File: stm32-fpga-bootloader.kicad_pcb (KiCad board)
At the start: 2 copper layers, 100 x 100 mm, 166 parts, among them J1 USB_C_Receptacle_USB2.0_14P, J10 LEDX, J11 LEDY, J12 PMOD, J13 Raspberry_Pi_2_3, J14 CPLD_JTAG, J2 Conn_01x02, J3 RPI-TO-CPLD, J5 PMOD, J6 Conn_01x02, J7 TO-LCD, J8 USB_C_Receptacle_USB2.0_14P, Q1 2N7002K, Q2 2N7002K, Q3 2N7002K, SW1 BOOT, SW2 RUN, SW3 ICE_BTN, SW4 ICE_RST, SW5 BOOT, U1 AMS1117-3.3, U10 RP2040, U2 W25Q128JVS, U3 LMV321, U4 ACPL-798J-500E, U5 ICE40UP5K-SG48ITR, U6 W25Q128JVS, U7 LP5907MFX-1.2, U8 MAX7221xNG, U9 LCMXO2-1200HC-4TG100I, Y1 12Mhz

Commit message: Update the source files
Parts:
- added C47: 4.7u, Capacitor_SMD:C_0603_1608Metric, F.Cu at (139.0, 120.0)
- added J4001: Conn_01x08, Connector_PinSocket_2.54mm:PinSocket_1x08_P2.54mm_Vertical, F.Cu at (159.3, 103.2)
- added Q4: 2N7002K, Package_TO_SOT_SMD:SOT-23, F.Cu at (122.2, 111.9)
- added Q5: 2N7002K, Package_TO_SOT_SMD:SOT-23, F.Cu at (143.5, 112.2)
- added Q6: 2N7002K, Package_TO_SOT_SMD:SOT-23, F.Cu at (126.6, 112.0)
- added Q7: 2N7002K, Package_TO_SOT_SMD:SOT-23, F.Cu at (147.6, 112.2)
- added R63: 10k, Resistor_SMD:R_0402_1005Metric, F.Cu at (135.9, 119.9)
- added R64: 10k, Resistor_SMD:R_0402_1005Metric, F.Cu at (123.0, 109.4)
- added R65: 330R, Resistor_SMD:R_0402_1005Metric, F.Cu at (123.0, 114.4)
- added R66: 330R, Resistor_SMD:R_0402_1005Metric, F.Cu at (144.3, 114.6)
- added R67: 10k, Resistor_SMD:R_0402_1005Metric, F.Cu at (144.3, 109.8)
- added R68: 10k, Resistor_SMD:R_0402_1005Metric, F.Cu at (125.8, 114.4)
- added R69: 330R, Resistor_SMD:R_0402_1005Metric, F.Cu at (125.8, 109.6)
- added R70: 10k, Resistor_SMD:R_0402_1005Metric, F.Cu at (148.3, 109.8)
- added R71: 330R, Resistor_SMD:R_0402_1005Metric, F.Cu at (148.3, 114.7)
- added TP1: TestPoint, TestPoint:TestPoint_Pad_1.0x1.0mm, F.Cu at (131.1, 120.3)
- added U11: 74HC595D, PCM_JLCPCB:SOIC-16_3.9x9.9mm_P1.27mm, F.Cu at (135.5, 112.1)
- added U12: LTC-3743KD, KiCadLocal:LTC-3743KD, F.Cu at (126.6, 117.2)
- moved C16 64.2 mm to (210.2, 87.1), turned to -90 degrees
- moved C15 43.2 mm to (208.8, 87.0), turned to -90 degrees
- moved C2 37.2 mm to (124.1, 83.4), turned to 180 degrees
- moved U2 30.3 mm to (125.7, 88.7), turned to 90 degrees
- moved R3 27.0 mm to (123.8, 94.5), turned to 0 degrees
- moved D11 26.9 mm to (116.6, 75.7)
- moved R6 26.6 mm to (120.1, 76.0)
- moved C10 23.4 mm to (141.8, 91.2)
- moved C44 23.4 mm to (137.8, 83.2)
- moved C7 23.4 mm to (144.0, 94.6)
- moved R1 23.4 mm to (130.7, 86.6)
- moved R12 23.4 mm to (141.8, 83.5)
- moved R2 23.4 mm to (130.8, 87.8)
- moved Y1 23.4 mm to (144.5, 88.1)
- moved C3 23.4 mm to (152.0, 83.3)
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
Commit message: Update the schematic
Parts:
- removed J4001: Conn_01x08, Connector_PinSocket_2.54mm:PinSocket_1x08_P2.54mm_Vertical
- added C48: 100n, Capacitor_SMD:C_0402_1005Metric, F.Cu at (122.6, 76.1)
- added C49: 10uF, Capacitor_SMD:C_0603_1608Metric, F.Cu at (125.5, 67.1)
- added J15: Conn_01x02, TerminalBlock_Phoenix:TerminalBlock_Phoenix_PT-1,5-2-3.5-H_1x02_P3.50mm_Horizontal, F.Cu at (117.9, 68.8)
- added J9: PMOD, Connector_PinSocket_2.54mm:PinSocket_2x06_P2.54mm_Vertical, F.Cu at (166.0, 78.0)
- added R72: 10k, Resistor_SMD:R_0402_1005Metric, F.Cu at (126.0, 131.8)
- added R73: 1.2K, Resistor_SMD:R_0603_1608Metric, F.Cu at (125.5, 69.6)
- added R74: 1.2K, Resistor_SMD:R_0603_1608Metric, F.Cu at (125.5, 72.1)
- added R75: 1.2K, Resistor_SMD:R_0603_1608Metric, F.Cu at (125.5, 74.6)
- added R76: 1.2K, Resistor_SMD:R_0603_1608Metric, F.Cu at (129.5, 67.1)
- added R77: 1.2K, Resistor_SMD:R_0603_1608Metric, F.Cu at (129.5, 69.6)
- added R78: 100R, Resistor_SMD:R_0603_1608Metric, F.Cu at (129.5, 72.1)
- added R79: 100R, Resistor_SMD:R_0603_1608Metric, F.Cu at (129.5, 74.6)
- added R80: 100R, Resistor_SMD:R_0603_1608Metric, F.Cu at (133.5, 67.1)
- added R81: 100R, Resistor_SMD:R_0603_1608Metric, F.Cu at (133.5, 69.6)
- added R82: 100R, Resistor_SMD:R_0603_1608Metric, F.Cu at (133.5, 72.1)
- added R83: 100R, Resistor_SMD:R_0603_1608Metric, F.Cu at (133.5, 74.6)
- added U1001: XC6206PxxxMR, Package_TO_SOT_SMD:SOT-23-3, F.Cu at (142.8, 120.6)
- added U13: ACPL-798J-500E, EasyEDA_Lib:SO-16_L10.3-W7.5-P1.27-LS10.6-BL, B.Cu at (129.9, 70.7)
- moved J2 90.6 mm to (226.0, 94.0)
- moved R13 74.6 mm to (244.8, 95.3)
- moved R15 74.6 mm to (248.2, 77.6)
- moved C11 74.6 mm to (236.7, 85.6)
- moved C12 74.6 mm to (236.7, 87.6)
- moved R14 74.6 mm to (234.3, 99.0)
- moved R16 74.6 mm to (248.2, 80.2)
- moved R17 74.6 mm to (234.3, 101.0)
- moved U3 74.6 mm to (232.7, 87.0)
- moved R18 74.6 mm to (234.3, 103.0)
- moved Q4 28.1 mm to (121.5, 83.8)
- moved Q5 28.1 mm to (142.8, 84.1)
- moved R63 28.1 mm to (135.2, 91.8)
- moved R64 28.1 mm to (122.3, 81.3)
- moved R65 28.1 mm to (122.3, 86.3)
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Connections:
- A2 pad 14: /CPLDK_SCK -> /CPLD_CLOCK
- U1 pad 1: GND -> unconnected-(U1-GND-Pad1)
- U1 pad 2: +3.3V_JTAG -> unconnected-(U1-VO-Pad2)
- U1 pad 3: /jtag-prog/VBUS -> unconnected-(U1-VI-Pad3)

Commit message: Update the schematic
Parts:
- removed J2: Conn_01x02, TerminalBlock_Phoenix:TerminalBlock_Phoenix_PT-1,5-2-3.5-H_1x02_P3.50mm_Horizontal
- added C50: 10uF, Capacitor_SMD:C_0603_1608Metric, F.Cu at (145.7, 66.8)
- added C51: 10uF, Capacitor_SMD:C_0603_1608Metric, F.Cu at (141.5, 66.7)
- added D1003: B5817W, PCM_JLCPCB:D_SOD-123, F.Cu at (137.5, 67.2)
- added D1004: B5817W, PCM_JLCPCB:D_SOD-123, F.Cu at (137.5, 69.7)
- added D1005: B5817W, PCM_JLCPCB:D_SOD-123, F.Cu at (137.5, 72.3)
- added J1001: DATA, Connector_PinSocket_2.54mm:PinSocket_1x04_P2.54mm_Vertical, F.Cu at (132.5, 67.1)
- J15: footprint TerminalBlock_Phoenix:TerminalBlock_Phoenix_PT-1,5-2-3.5-H_1x02_P3.50mm_Horizontal -> Connector_PinSocket_2.54mm:PinSocket_1x02_P2.54mm_Vertical
- U11: footprint PCM_JLCPCB:SOIC-16_3.9x9.9mm_P1.27mm -> PCM_JLCPCB:SOIC-16_L9.9-W3.9-P1.27-LS6.0-BL
- moved R16 94.9 mm to (153.3, 79.8)
- moved R13 94.2 mm to (151.5, 82.5)
- moved R15 92.0 mm to (156.5, 85.1)
- moved R14 82.6 mm to (153.0, 84.5)
- moved R17 82.6 mm to (153.0, 86.5)
- moved R18 82.6 mm to (153.0, 88.5)
- moved C11 78.2 mm to (158.6, 80.8)
- moved C12 78.2 mm to (158.6, 82.8)
- moved U3 78.2 mm to (154.6, 82.2)
- moved U1 35.0 mm to (143.6, 72.1)
- moved U1001 16.2 mm to (150.8, 106.5)
- moved R73 10.5 mm to (115.6, 66.0)
- moved R77 10.1 mm to (119.7, 72.0), turned to -90 degrees
- moved C49 9.58 mm to (128.1, 76.3), turned to 180 degrees
- moved R74 8.94 mm to (119.0, 65.9)
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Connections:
- net /jtag-prog/VBUS renamed VBUS3
- A1 pad 40: unconnected-(A1-VBUS-Pad40) -> VBUS1
- A2 pad 40: unconnected-(A2-VBUS-Pad40) -> VBUS2
- U1 pad 1: unconnected-(U1-GND-Pad1) -> GND
- U1 pad 2: unconnected-(U1-VO-Pad2) -> Net-(U1-VO)
- U1 pad 3: unconnected-(U1-VI-Pad3) -> Net-(U1-VI)

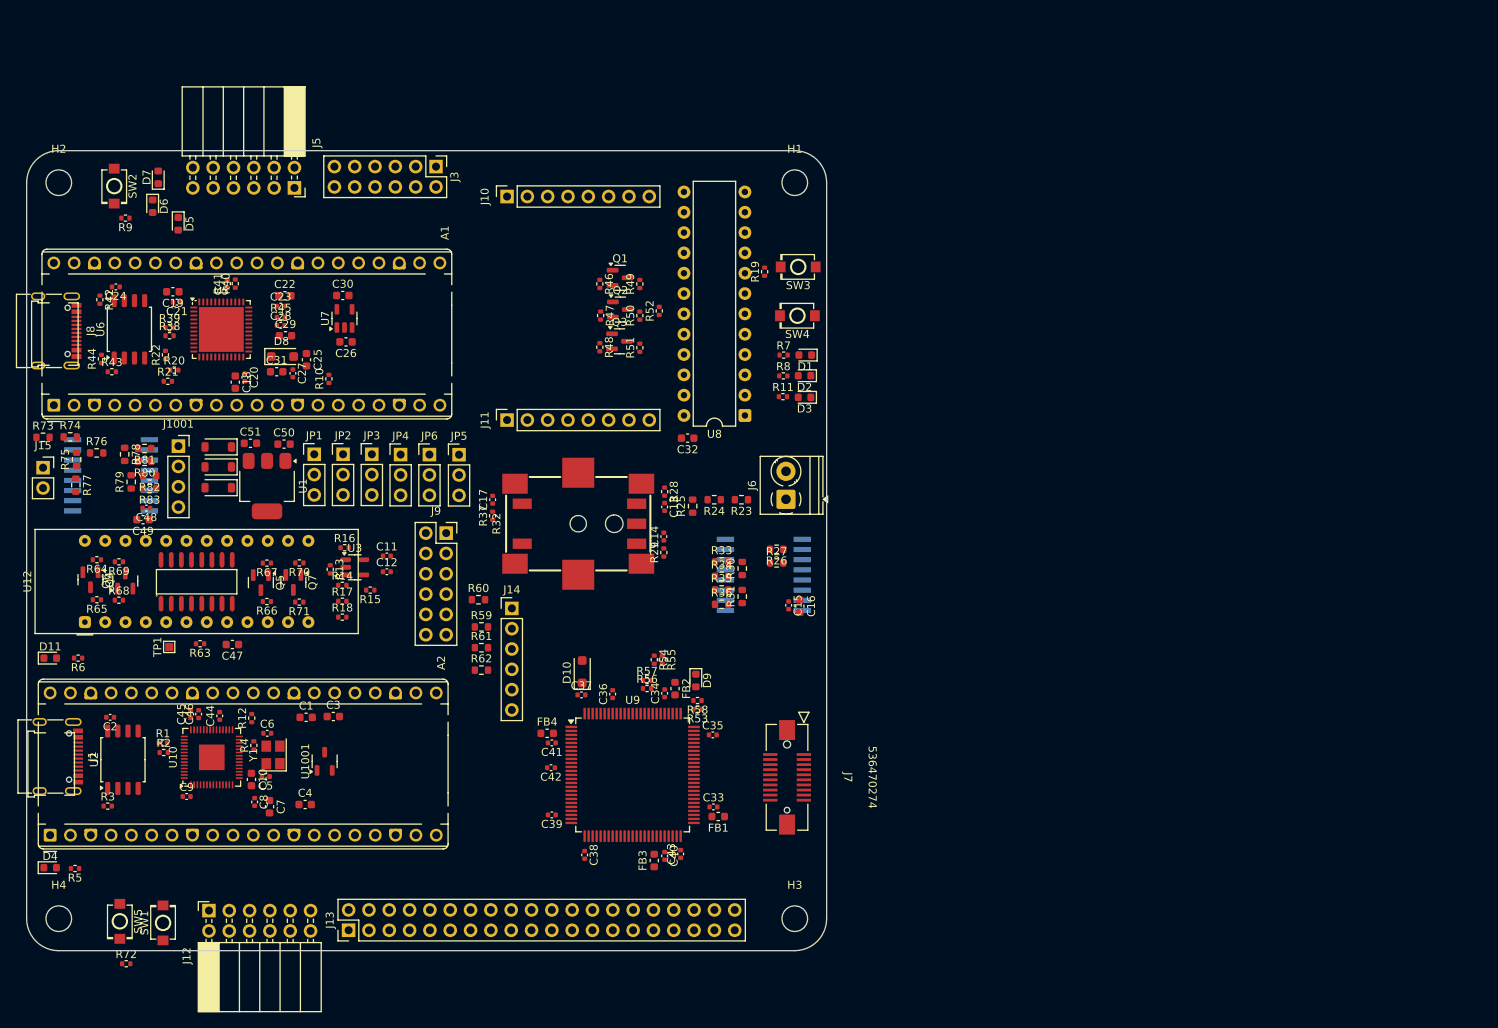
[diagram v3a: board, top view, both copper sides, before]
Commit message: Update the footprints
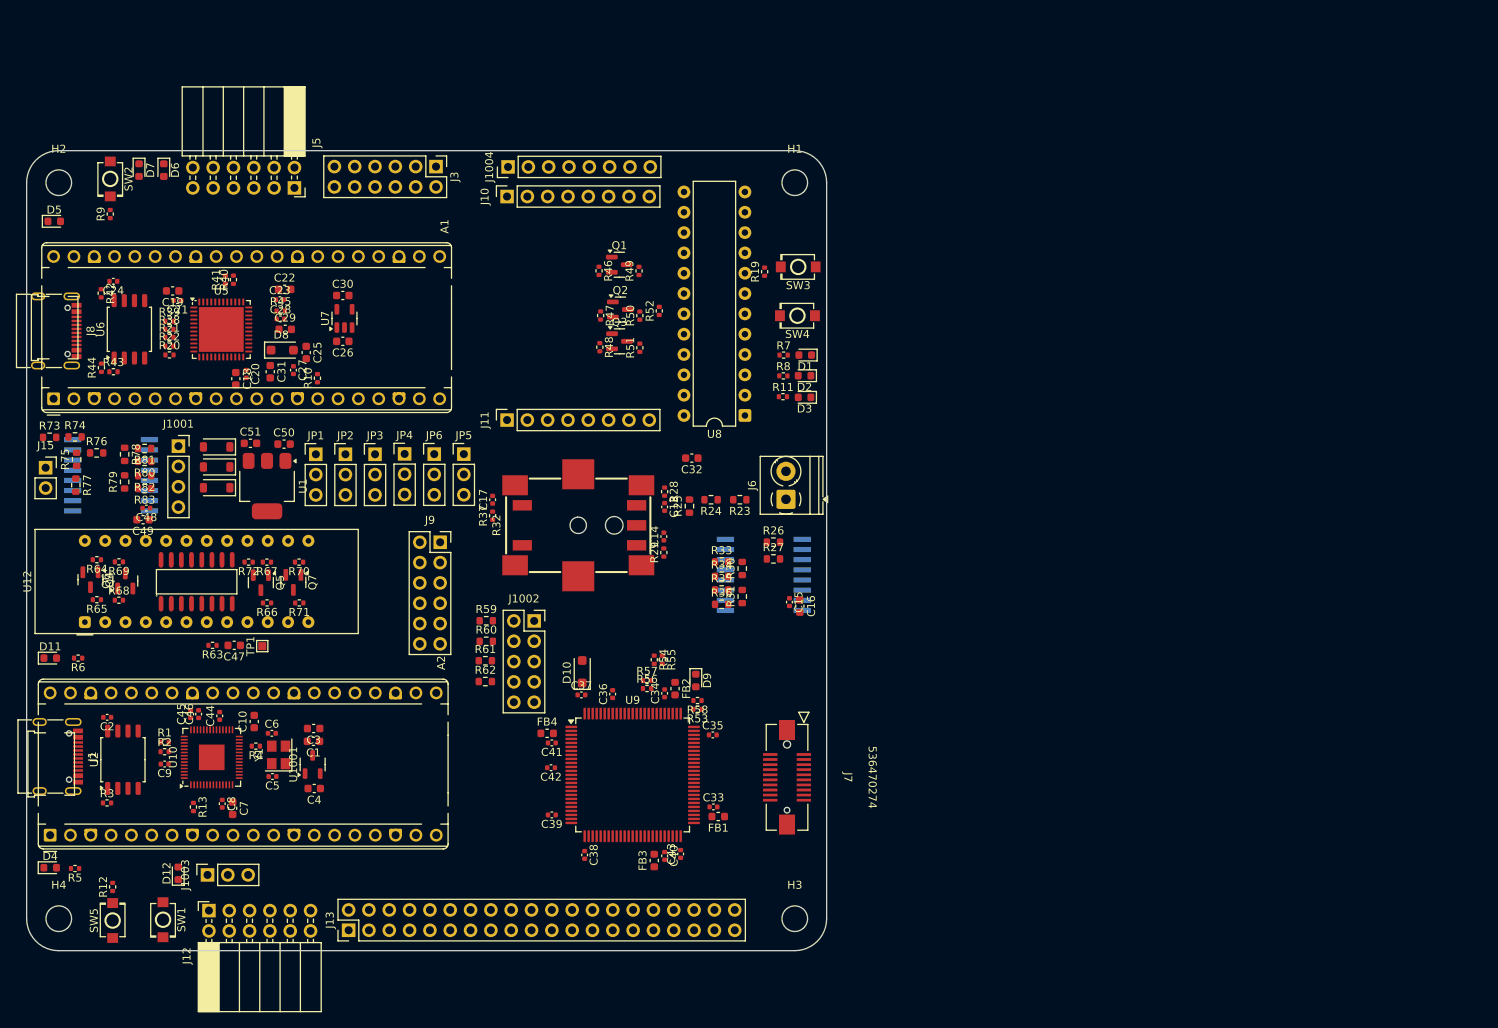
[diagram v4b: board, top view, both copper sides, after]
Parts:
- removed C11, C12: 100n, Capacitor_SMD:C_0402_1005Metric
- removed J14: CPLD_JTAG, Connector_PinHeader_2.54mm:PinHeader_1x06_P2.54mm_Vertical
- removed R14, R15, R16, R17, R18: 1.2K, Resistor_SMD:R_0402_1005Metric
- removed U3: LMV321, Package_TO_SOT_SMD:SOT-23-5
- added D12: RED, LED_SMD:LED_0603_1608Metric, F.Cu at (132.5, 120.5)
- added J1002: JTAG JUMP, Connector_PinSocket_2.54mm:PinSocket_2x05_P2.54mm_Vertical, F.Cu at (177.0, 88.9)
- added J1003: JTAG-LOG, Connector_PinSocket_2.54mm:PinSocket_1x03_P2.54mm_Vertical, F.Cu at (136.2, 120.7)
- added J1004: Conn_01x08, Connector_PinHeader_2.54mm:PinHeader_1x08_P2.54mm_Vertical, F.Cu at (173.7, 32.2)
- R13: value 1R -> 1.2K
- moved R72 52.5 mm to (141.3, 81.6), turned to 180 degrees
- moved R13 34.3 mm to (134.4, 112.2)
- moved R12 27.3 mm to (124.3, 122.2)
- moved D5 15.5 mm to (117.0, 39.0), turned to 0 degrees
- moved TP1 11.6 mm to (143.0, 92.1)
- moved C10 7.26 mm to (142.0, 101.5), turned to 90 degrees
- moved R21 5.50 mm to (131.4, 53.5)
- moved R60 5.29 mm to (171.0, 91.5)
- moved C9 4.90 mm to (130.8, 106.8), turned to 180 degrees
- moved D6 4.72 mm to (130.7, 32.6)
- moved C7 4.62 mm to (139.3, 112.4)
- moved C8 4.06 mm to (138.0, 111.8)
- moved C1 3.14 mm to (149.4, 104.0), turned to 180 degrees
- moved C3 2.88 mm to (149.4, 102.4), turned to 180 degrees
- moved D7 2.56 mm to (127.6, 32.6), turned to -90 degrees
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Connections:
- A1 pad 11: /UART1_TX -> /IOB_23b
- A1 pad 12: /UART1_RX -> /IOT_43a
- A1 pad 33: GND -> unconnected-(A1-AGND-Pad33)
- A1 pad 34: unconnected-(A1-GPIO28_ADC2-Pad34) -> /LED1
- C50 pad 1: Net-(U1-VO) -> +3.3V
- C51 pad 1: Net-(U1-VI) -> +5V
- D1003 pad 1: Net-(U1-VI) -> +5V
- D1004 pad 1: Net-(U1-VI) -> +5V
- D1005 pad 1: Net-(U1-VI) -> +5V
- R11 pad 1: /LED2 -> /IOT_50b
- R13 pad 1: Net-(R13-Pad1) -> /jtag-prog/LED2
- R32 pad A: /ENCODER_B -> /ENCODER_A
- R32 pad B: /ENCODER_A -> /ENCODER_B
- R32 pad D: GND -> /ENCODER_BTN
- R32 pad E: /ENCODER_BTN -> GND
- R59 pad 2: /PT10D/TDI -> /TDI
- R60 pad 2: /PT10C/TDO -> /TDO
- R61 pad 2: /PT11C/TCK -> /TCK
- R62 pad 2: /PT11D/TMS -> /TMS
- U1 pad 2: Net-(U1-VO) -> +3.3V
- U1 pad 3: Net-(U1-VI) -> +5V
- U10 pad 2: unconnected-(U10-GPIO0-Pad2) -> /jtag-prog/LED2

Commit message: Update the BOM and the routing
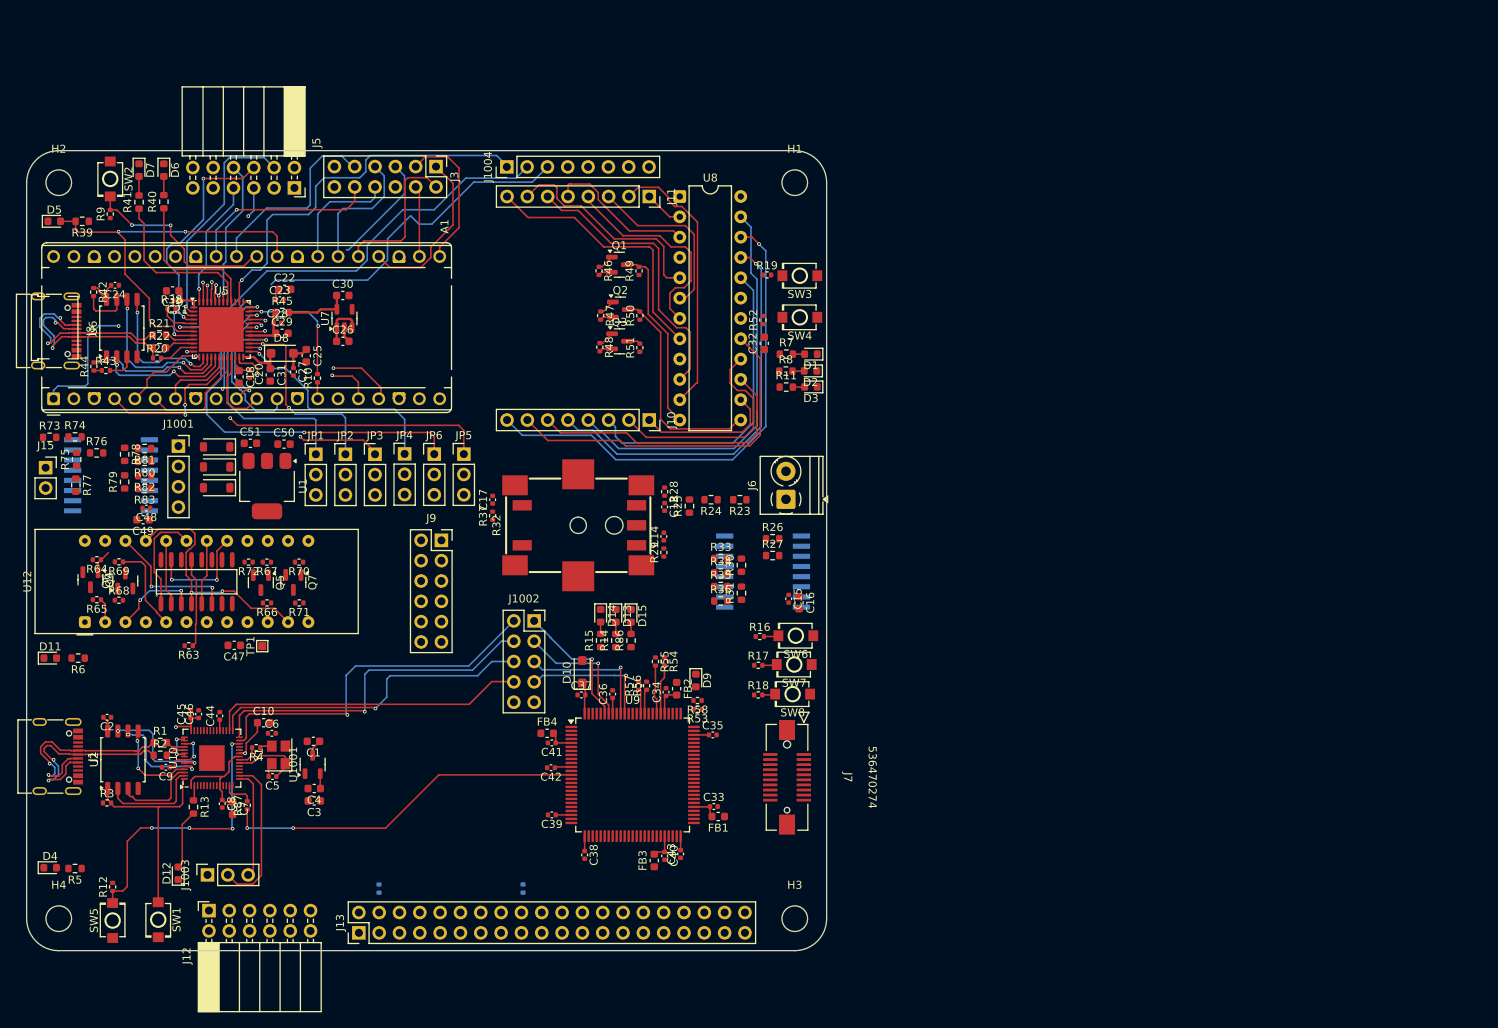
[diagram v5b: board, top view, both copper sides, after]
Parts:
- removed A2: RaspberryPi_Pico, Module:RaspberryPi_Pico_Common_THT
- removed R59, R60, R61, R62: 0R, Resistor_SMD:R_0603_1608Metric
- added D13: RED, LED_SMD:LED_0603_1608Metric, F.Cu at (187.2, 88.3)
- added D14: RED, LED_SMD:LED_0603_1608Metric, F.Cu at (185.3, 88.3)
- added D15: RED, LED_SMD:LED_0603_1608Metric, F.Cu at (189.1, 88.3)
- added R14: 1.2K, Resistor_SMD:R_0603_1608Metric, F.Cu at (187.2, 91.4)
- added R15: 1.2K, Resistor_SMD:R_0603_1608Metric, F.Cu at (185.3, 91.4)
- added R16: 10k, Resistor_SMD:R_0402_1005Metric, F.Cu at (205.2, 90.9)
- added R17: 10k, Resistor_SMD:R_0402_1005Metric, F.Cu at (205.0, 94.5)
- added R18: 10k, Resistor_SMD:R_0402_1005Metric, F.Cu at (205.0, 98.2)
- added R84: 0R, Resistor_SMD:R_0402_1005Metric, B.Cu at (175.6, 122.4)
- added R85: 0R, Resistor_SMD:R_0402_1005Metric, B.Cu at (157.6, 122.4)
- added R86: 1.2K, Resistor_SMD:R_0603_1608Metric, F.Cu at (189.1, 91.4)
- added R87: 10R, Resistor_SMD:R_0402_1005Metric, F.Cu at (141.1, 112.0)
- added SW6: BTN, EasyEDA_Lib:SW-SMD_L3.9-W3.0-P4.45, F.Cu at (209.7, 90.8)
- added SW7: BTN, EasyEDA_Lib:SW-SMD_L3.9-W3.0-P4.45, F.Cu at (209.5, 94.4)
- added SW8: BTN, EasyEDA_Lib:SW-SMD_L3.9-W3.0-P4.45, F.Cu at (209.3, 98.1)
- C10, C18, C19, C22, C25, C26, C29, C30, C32, C47, C7: value 4.7u -> 4.7uF
- R1, R11, R13, R2, R21, R22, R39, R40, R41, R45, R5, R6, R7, R8: footprint Resistor_SMD:R_0402_1005Metric -> Resistor_SMD:R_0603_1608Metric
- moved J10 33.1 mm to (191.4, 63.8), turned to -90 degrees
- moved J11 33.1 mm to (191.4, 35.9), turned to -90 degrees
- moved U8 28.6 mm to (195.2, 35.9), turned to 0 degrees
- moved C32 17.0 mm to (205.8, 54.2), turned to 90 degrees
- moved R39 16.6 mm to (120.5, 39.0), turned to 180 degrees
- moved R41 14.5 mm to (127.6, 36.6)
- moved R40 13.1 mm to (130.7, 36.5)
- moved R52 13.0 mm to (205.6, 51.3)
- moved C3 9.05 mm to (149.5, 111.4)
- moved R63 2.98 mm to (133.8, 92.0)
- moved R38 2.56 mm to (131.7, 49.9)
- moved R20 1.60 mm to (129.9, 56.1)
- moved D3 1.53 mm to (211.6, 59.7)
- moved J13 1.32 mm to (155.1, 127.9)
- moved R54 1.29 mm to (193.3, 94.0)
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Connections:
- C26 pad 1: VBUS -> +5V
- J13 pad 1: unconnected-(J13-3V3-Pad1)_1 -> Net-(J13-3V3-Pad1)
- J13 pad 17: unconnected-(J13-3V3-Pad1) -> Net-(J13-3V3-Pad1)
- J13 pad 2: unconnected-(J13-5V-Pad2)_1 -> Net-(J13-5V-Pad2)
- J13 pad 4: unconnected-(J13-5V-Pad2) -> Net-(J13-5V-Pad2)
- U10 pad 13: unconnected-(U10-GPIO10-Pad13) -> Net-(U10-GPIO10)
- U10 pad 27: /jtag-prog/TDI -> /TDI
- U10 pad 28: /jtag-prog/TDO -> /TDO
- U10 pad 29: /jtag-prog/TCK -> /TCK
- U10 pad 30: /jtag-prog/TMS -> /TMS
- U7 pad 1: VBUS -> +5V
- U7 pad 3: VBUS -> +5V
- U9 pad 1: unconnected-(U9-PL2C/L_GPLLT_IN-Pad1) -> /lcmxo2-cpld-block/PL2C/L_GPLLT_IN
- U9 pad 13: /lcmxo2-cpld-block/PL5B/PCLKC3_1 -> /jtag-prog/CLK
- U9 pad 2: unconnected-(U9-PL2D/L_GPLLC_IN-Pad2) -> /lcmxo2-cpld-block/PL2D/L_GPLLC_IN
- U9 pad 3: unconnected-(U9-PL3A/PCLKT3_2-Pad3) -> /lcmxo2-cpld-block/PL3A/PCLKT3_2
- U9 pad 7: unconnected-(U9-PL3C-Pad7) -> /lcmxo2-cpld-block/PL3C
- U9 pad 8: unconnected-(U9-PL3D-Pad8) -> /lcmxo2-cpld-block/PL3D
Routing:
- net Net-(J10-Pin_8): track 0.00 -> 61.9 mm, vias 0 -> 1
- net /IOB_13b: track 0.00 -> 54.5 mm, vias 0 -> 1
- net /ICE_SPI_SCK: track 0.00 -> 52.0 mm, vias 0 -> 2
- net /IOT_48b: track 0.00 -> 50.8 mm, vias 0 -> 3
- net Net-(J10-Pin_4): track 0.00 -> 50.7 mm
- net Net-(J10-Pin_5): track 0.00 -> 50.2 mm, vias 0 -> 1
- net /ICE_CDONE: track 0.00 -> 49.9 mm, vias 0 -> 2
- net /IOT_45a_G1: track 0.00 -> 49.0 mm, vias 0 -> 2
- net /IOT_50b: track 0.00 -> 48.8 mm, vias 0 -> 1
- net /IOT_37a: track 0.00 -> 47.2 mm, vias 0 -> 1
- net /ICE_SPI_SS: track 0.00 -> 46.5 mm, vias 0 -> 3
- net /jtag-prog/CLK: track 0.00 -> 45.6 mm, vias 0 -> 2
- net /TDI: track 0.00 -> 45.3 mm, vias 0 -> 1
- net Net-(J10-Pin_7): track 0.00 -> 44.1 mm
- net /TDO: track 0.00 -> 43.7 mm, vias 0 -> 1
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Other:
- copper layers 2 -> 4
